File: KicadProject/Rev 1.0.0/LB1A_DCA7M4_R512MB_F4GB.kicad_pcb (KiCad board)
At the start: 6 copper layers, 50 x 50 mm, 156 parts, among them U1 TFBGA361_12X12, U2 AS4C256M16D3LC-12BCN, U3 S40FC004C1B2C00000, U4 STPMIC1BPQR, U5 DF40C-70DP-0.4V(51), U6 DF40C-70DP-0.4V(51), U7 DF40C-70DP-0.4V(51), U8 LBEE59B1LV-278, X1 32.768kHz, X2 24MHz

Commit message: Design Complete
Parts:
- added G***: LOGO, U_Logos:logicboards_pcb_logo, F.Cu at (119.4, 78.5)
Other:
- board text added: "Logicboard 1A Rev 1.0.0 www.logicboards.org"
- board text removed: "LOGIC BOARD 1A LB1A_DCA7M4_R512MB_F4GB REV 1.0.0"

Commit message: Generated Fab Files
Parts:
- moved H1 57.7 mm to (60.5, 63.0)
- moved G*** 57.1 mm to (62.5, 74.0)
- moved C16 57.1 mm to (100.6, 74.3)
- moved C17 57.1 mm to (100.6, 76.5)
- moved C36 57.1 mm to (96.9, 80.7)
- moved C39 57.1 mm to (79.1, 93.0)
- moved C40 57.1 mm to (79.1, 100.6)
- moved C49 57.1 mm to (80.5, 85.5)
- moved C56 57.1 mm to (71.3, 85.4)
- moved C63 57.1 mm to (86.7, 98.2)
- moved C65 57.1 mm to (88.6, 101.1)
- moved C75 57.1 mm to (89.3, 106.6)
- moved L3 57.1 mm to (77.9, 86.1)
- moved L5 57.1 mm to (103.6, 61.2)
- moved R1 57.1 mm to (87.8, 89.2)
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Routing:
- net GND: track 210.0 -> 208.0 mm, vias 187 -> 188
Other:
- board text added: "3.5 MILS 3 MILS 15.75 MILS 7.9 MILS 10.85 MILS 3.95 MILS 5 MILS 4 MILS"
- board text added: "4 x Radius 2.4mm"
- board text added: ": : : : : : :"
- board text added: ": : : : : : : :"
- board text added: "A. MATERIAL B. SOLDERMASK COLOR C. SILKSCREEN COLOR D. SURFACE FINISH E. IMPEDANCE CONTROL F. VIAS G. STACKUP"
- board text added: "CONSTANT NA 3.5 - 4.29 - 4.29 - 4.29 - 4.29 - 4.29 - 3.5 NA"
- board text added: "COUNT 547 2 100 25"
- board text added: "DEFAULT:"
- board text added: "DRILL LAYER TopL - BottomL TopL - BottomL TopL - SignalL1 BottomL - SignalL4"
- board text added: "DRILL TABLE:"
- board text added: "FR-4(TG-150) MATT BLACK WHITE ENIG (GOLD) NA SEE DRILL TABLE SEE STACKUP TABLE"
- board text added: "HOLE SIZE 0.201 mm 2.200 mm 0.100 mm 0.100 mm"
- board text added: "HOLE TYPE Round Slot Round Round"
- board text added: "LAYER 1 2 3 4 5 6 7 8 9 10 11 12 13 14 15"
- board text added: "LAYER STACKUP:"
- board text added: "MATERIAL - Solder Resist Copper FR-4 Copper FR-4 Copper FR-4 Copper FR-4 Copper FR-4 Copper Solder Resist -"
- board text added: "MINIMUM PARAMETERS:"
- board text added: "NAME Top Overlay Top Solder Top Layer Dielectric 1 Signal Layer 1 Dielectric 2 Signal Layer 2 Dielectric 3 Signal Layer 3 Dielectric 4 Signal Layer 4 Dielectric 5 Bottom Layer Bottom Solder Bottom Overlay"
- board text added: "PCB SPECIFICATIONS:"
- board text added: "PLATED PTH PTH PTH PTH"
- board text added: "Refer Drill_Report.txt"
- board text added: "THICKNESS - 0.020 mm 0.035 mm 0.11 mm 0.035 mm 0.6 mm 0.035 mm 0.11 mm 0.035 mm 0.11 mm 0.035 mm 0.6 mm 0.035 mm 0.020 mm -"
- board text added: "TRACE WIDTH CLEARANCE VIA SIZE VIA DRILL uVIA SIZE uVIA DRILL dPAIR WIDTH dPAIR GAP"
- board text added: "Total Board Thickness - 1.6mm Tolerance - 10% Note - Manufacturer follow their own standard 1.6mm thickness stackup."

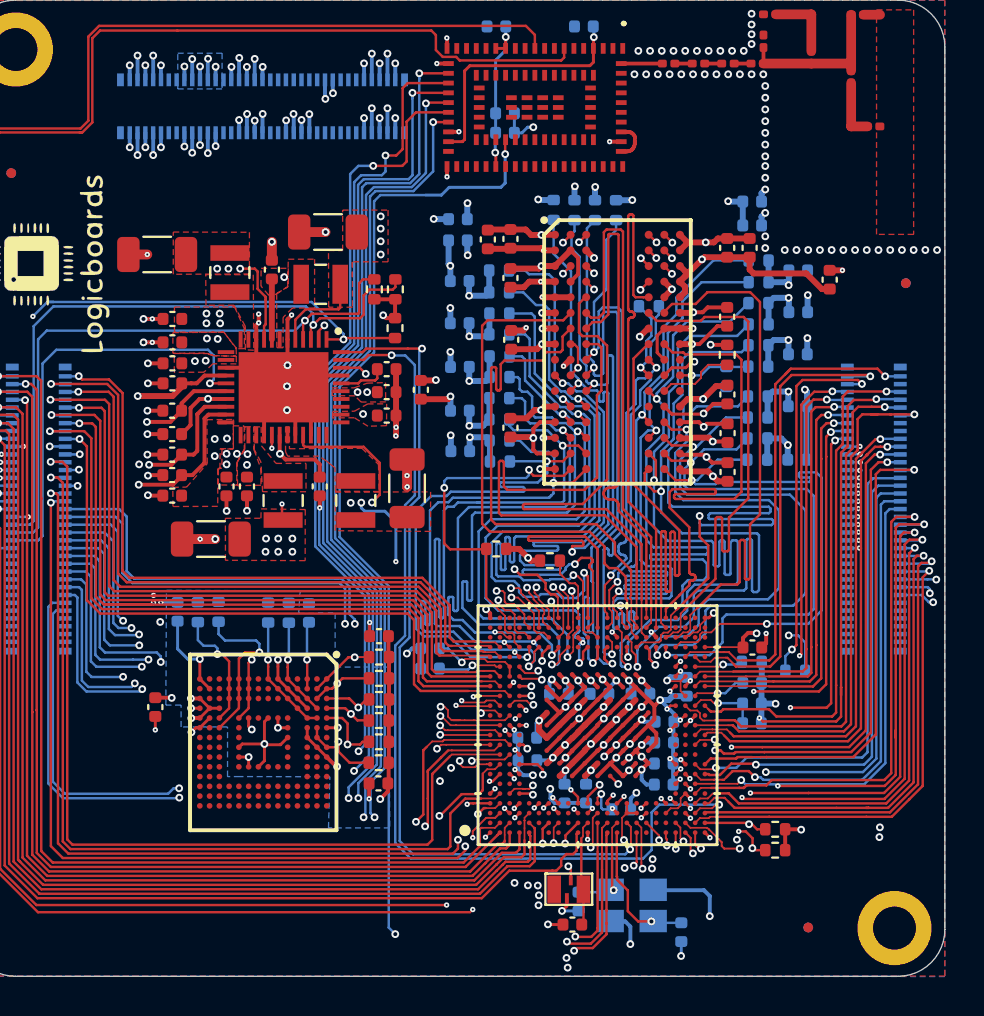
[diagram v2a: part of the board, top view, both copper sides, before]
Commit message: added assembly diagrams
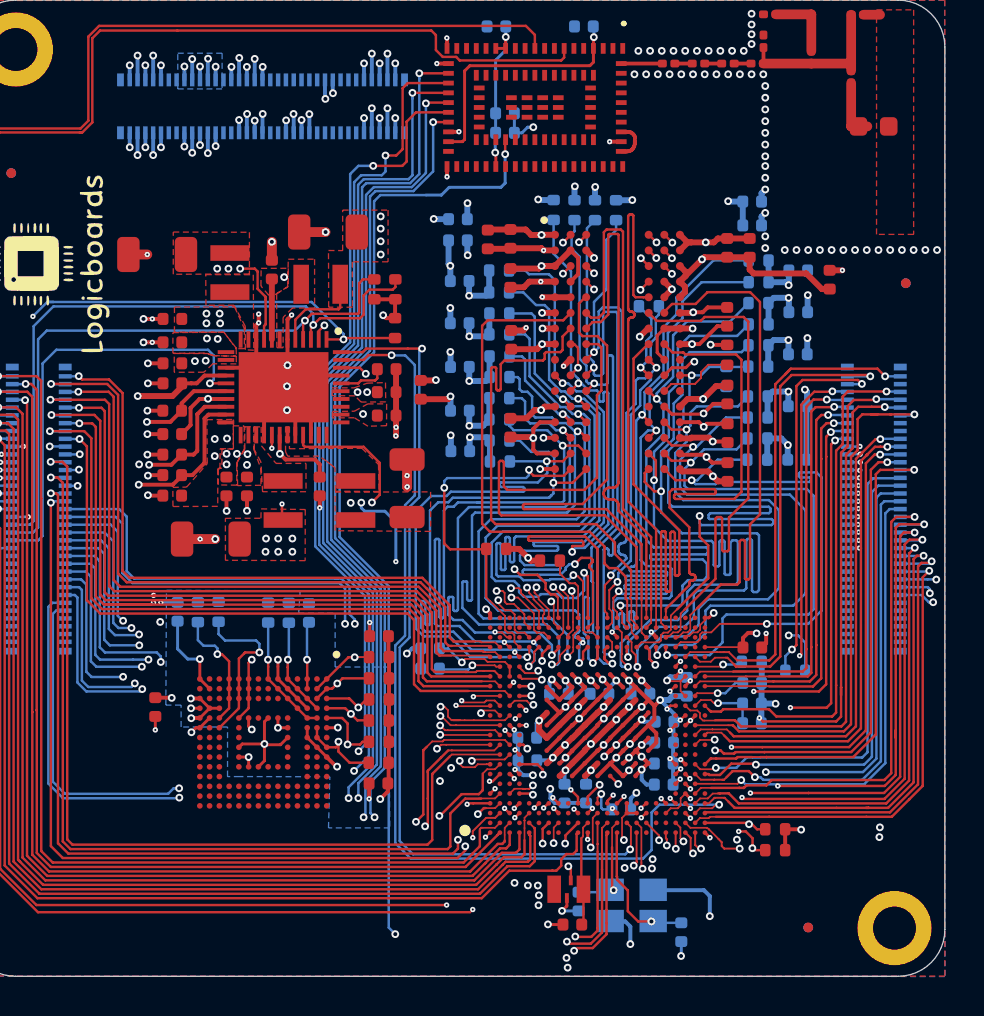
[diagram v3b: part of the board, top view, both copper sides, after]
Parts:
- C1, C10, C11, C12, C13, C14, C15, C16, C17, C18, C19, C2, C20, C21, C22, C23, C24, C25, C26, C27, C28, C29, C3, C30, C31, C32, C34, C35, C36, C37, C38, C39, C4, C40, C41, C42, C43, C44, C45, C46, C5, C51, C52, C53, C54, C55, C56, C57, C58, C59, C6, C60, C61, C62, C63, C64, C65, C66, C67, C68, C69, C7, C70, C72, C73, C74, C75, C76, C77, C79, C8, C85, C86, C9: footprint Capacitor_SMD:C_0402_1005Metric -> U_Capacitor_SMD:C_0402_1005Metric
- C33: footprint Capacitor_SMD:C_0201_0603Metric -> U_Capacitor_SMD:C_0603_1608Metric
- C47, C48, C49, C50: footprint Capacitor_SMD:C_1206_3216Metric -> U_Capacitor_SMD:C_1206_3216Metric
- C71, C78: footprint Capacitor_SMD:C_0201_0603Metric -> U_Capacitor_SMD:C_0201_0603Metric
- FID1, FID2, FID3, FID4, FID5, FID6: footprint Fiducial:Fiducial_0.5mm_Mask1.5mm -> U_Fiducial:Fiducial_0.5mm_Mask1.5mm
- H1, H3: footprint MountingHole:MountingHole_2.2mm_M2_DIN965_Pad -> U_MountingHole:MountingHole_2.2mm_M2_DIN965_Pad
- L5, L6, L7, L8: footprint Inductor_SMD:L_0201_0603Metric -> U_Inductor_SMD:L_0201_0603Metric
- R1, R10, R11, R12, R13, R14, R15, R16, R17, R18, R19, R2, R20, R21, R22, R23, R24, R25, R26, R27, R28, R29, R3, R30, R31, R32, R33, R34, R35, R36, R37, R38, R39, R4, R40, R41, R42, R43, R44, R45, R46, R5, R6, R7, R8, R9: footprint Resistor_SMD:R_0402_1005Metric -> U_Resistor_SMD:R_0402_1005Metric
- R47, R48, R49: footprint Resistor_SMD:R_0201_0603Metric -> U_Resistor_SMD:R_0201_0603Metric
